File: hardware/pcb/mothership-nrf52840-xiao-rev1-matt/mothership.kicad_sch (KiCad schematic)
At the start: 0 parts

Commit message: pcb: tmp update
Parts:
- added U1: XIAO_nRF52840, symbol A9M0330:MCU_Module__XIAO_nRF52840_NFC-NC
- added U2, U3: MCP23017x-x-SS, Package_SO:SSOP-28_5.3x10.2mm_P0.65mm, symbol A9M0330:IO_Expansion__MCP23017x-x-SS

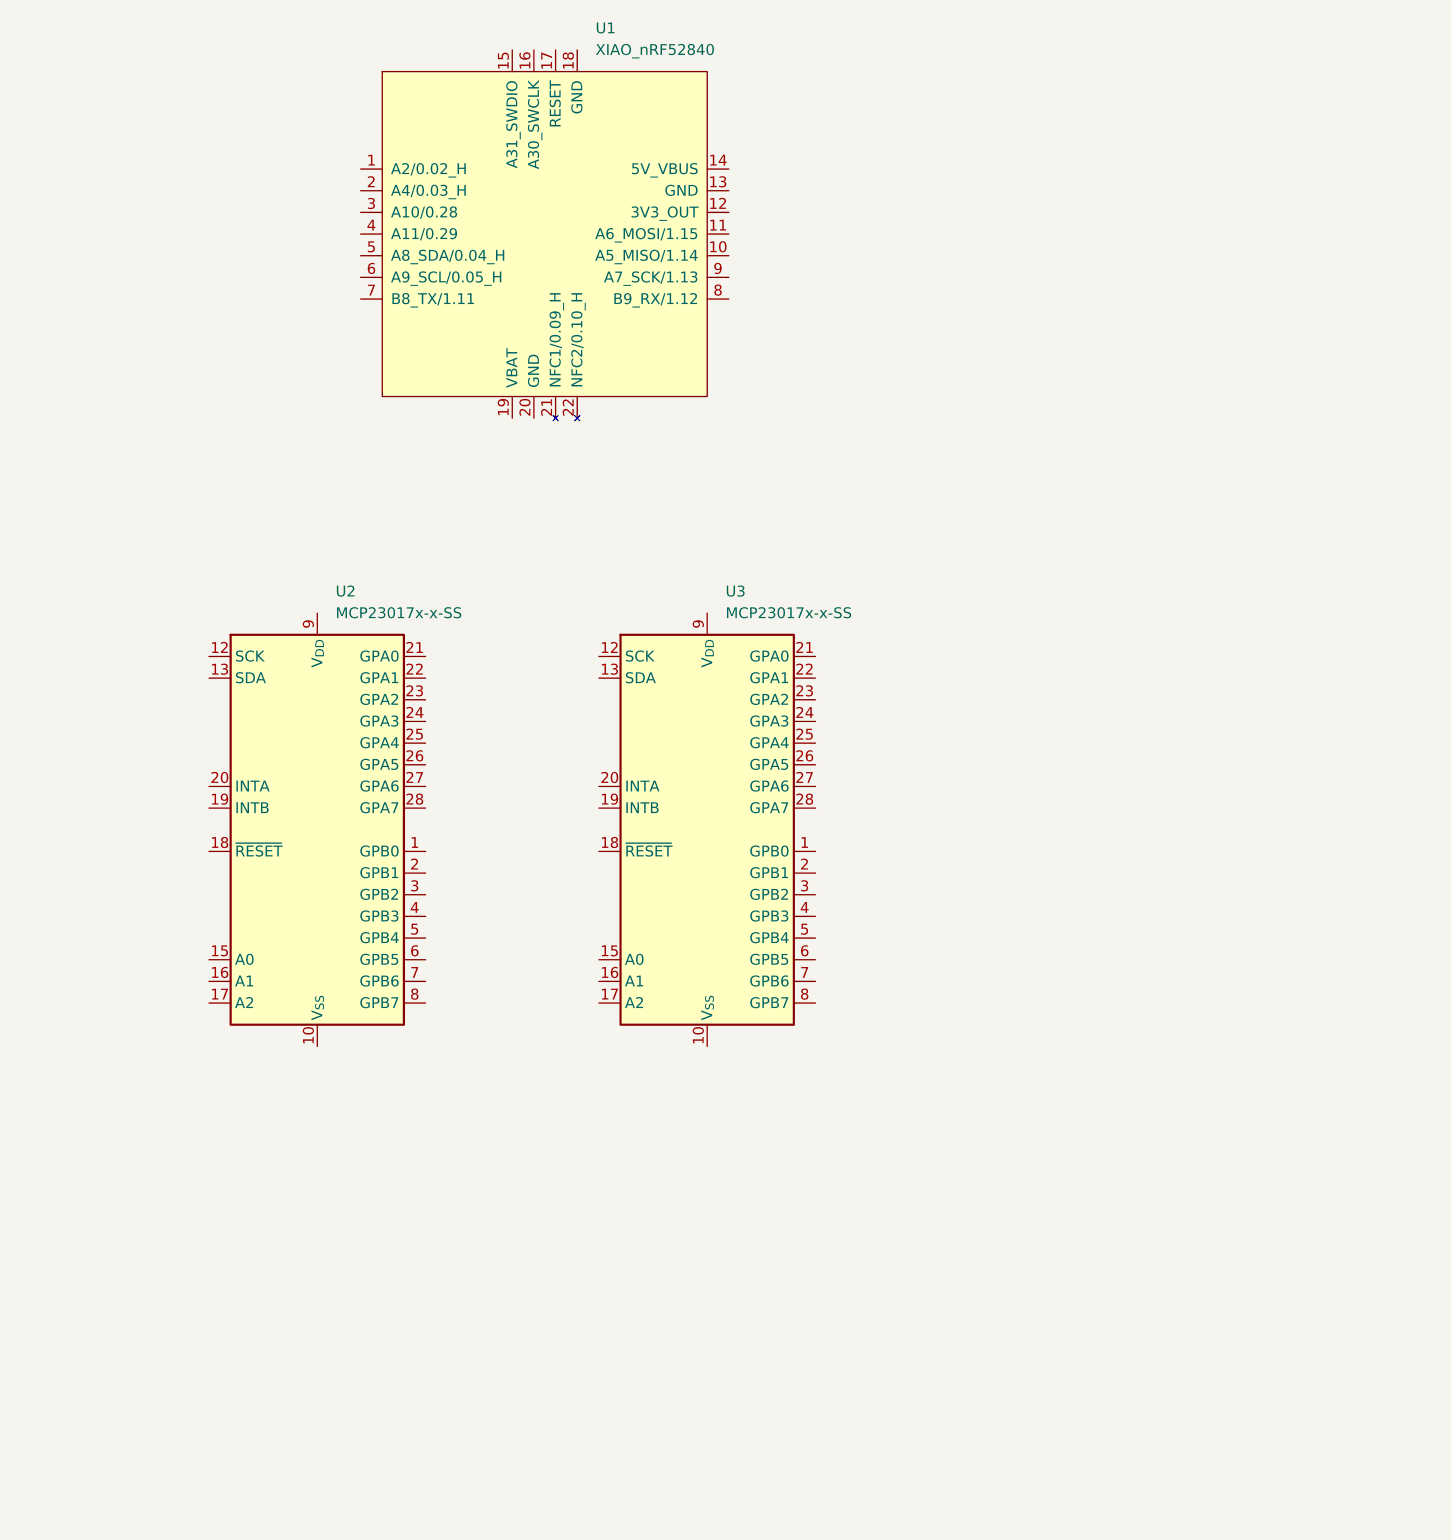
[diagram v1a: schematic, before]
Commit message: sch: add io expander matrix wiring
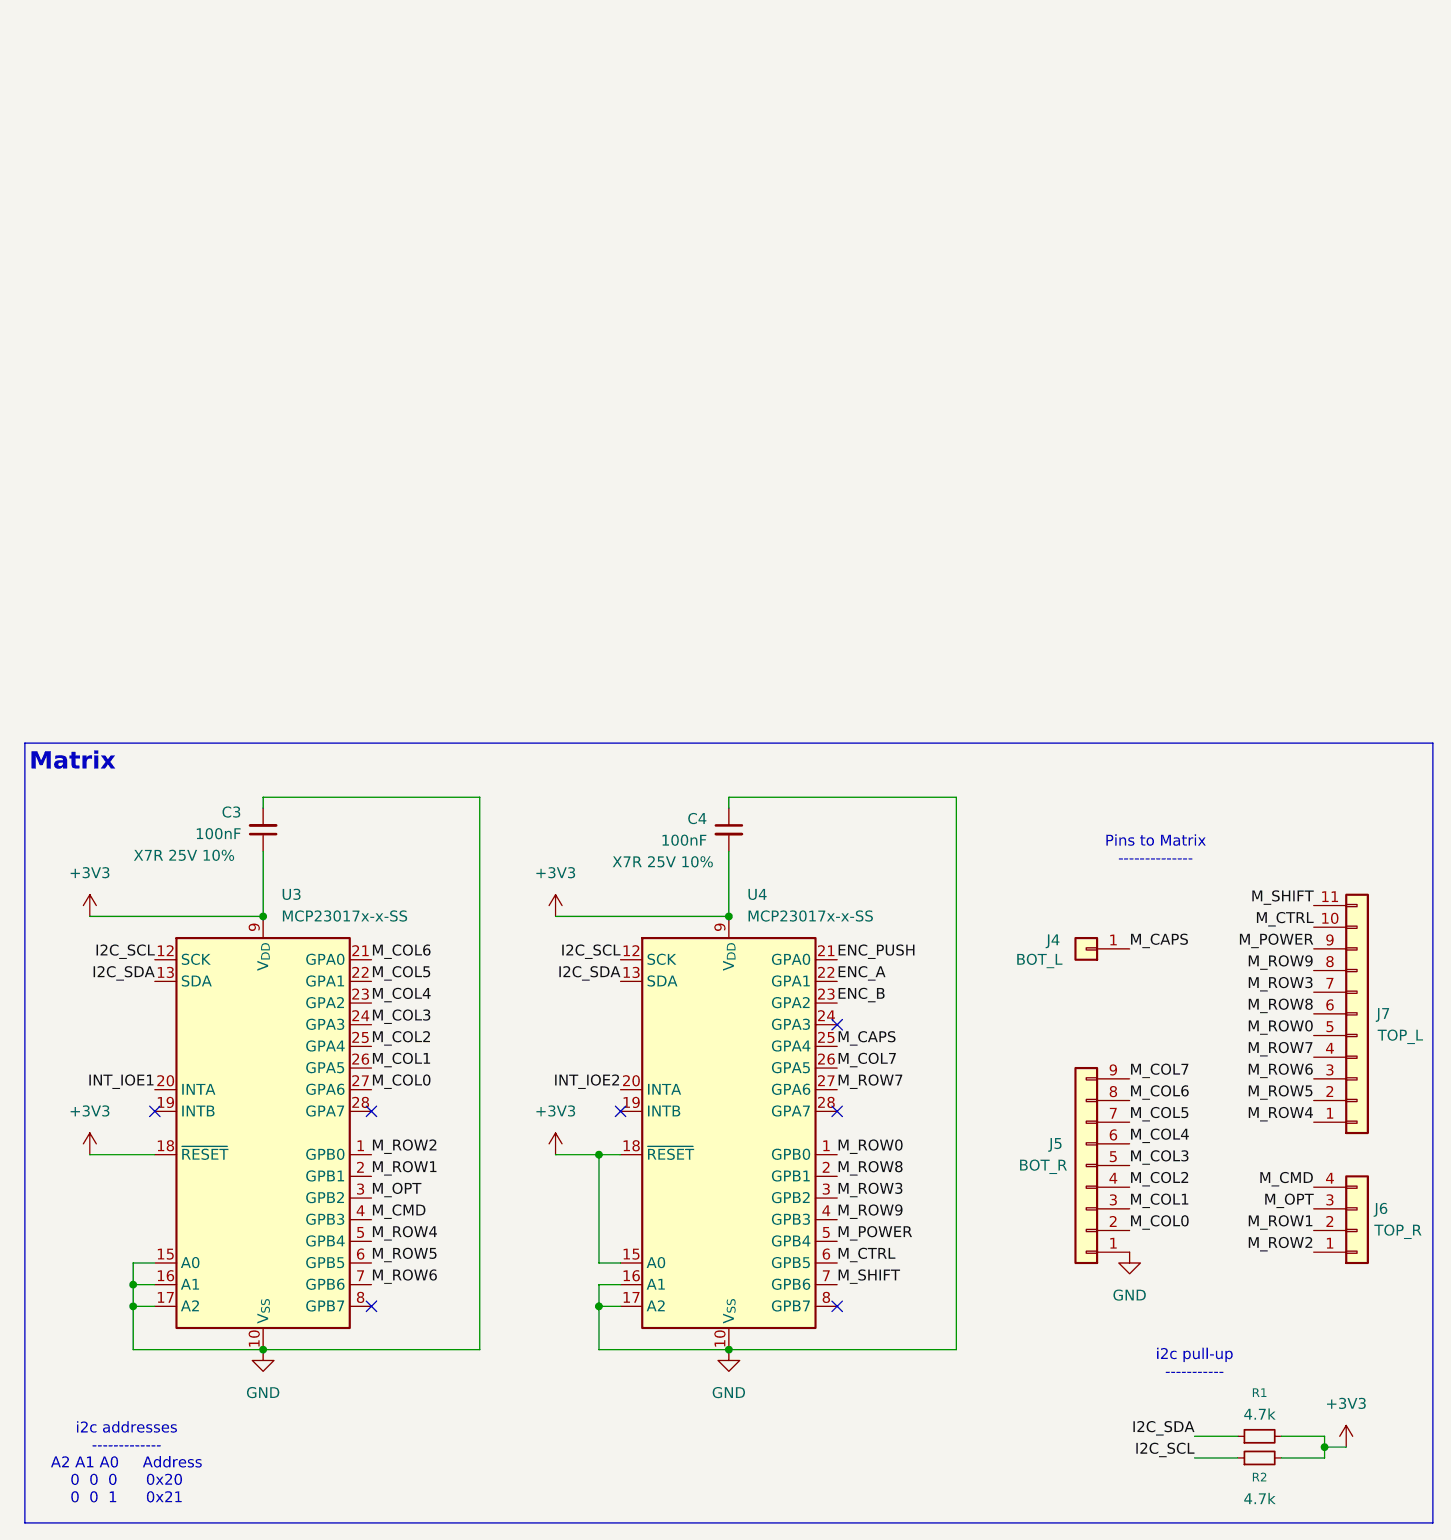
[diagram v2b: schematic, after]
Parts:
- removed U1: XIAO_nRF52840, symbol A9M0330:MCU_Module__XIAO_nRF52840_NFC-NC
- added C3, C4: 100nF, symbol A9M0330:C_Small
- added J4: BOT_L, symbol A9M0330:Conn_01x01
- added J5: BOT_R, symbol A9M0330:Conn_01x09
- added J6: TOP_R, symbol A9M0330:Conn_01x04
- added J7: TOP_L, symbol A9M0330:Conn_01x11
- added R1, R2: 4.7k, symbol A9M0330:R_Small
- renumbered U2 to U3, U3 to U4
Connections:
- net M_ROW2: now reaches U3.1 (GPB0)
- net M_ROW2: now also J6.1 (Pin_1)
- net GND: now reaches U3.10 (V_{SS})
- net GND: now also U3.15 (A0), U3.16 (A1), U3.17 (A2), U4.10 (V_{SS}), U4.16 (A1), U4.17 (A2), C3.2, C4.1, J5.1 (Pin_1)
- net I2C_SCL: now reaches U3.12 (SCK)
- net I2C_SCL: now also U4.12 (SCK), R2.1
- net I2C_SDA: now reaches U3.13 (SDA)
- net I2C_SDA: now also U4.13 (SDA), R1.1
- net +3V3: now reaches U3.18 (~{RESET})
- net +3V3: now also U3.9 (V_{DD}), U4.15 (A0), U4.18 (~{RESET}), U4.9 (V_{DD}), C3.1, C4.2, R1.2, R2.2
- net M_ROW1: now reaches U3.2 (GPB1)
- net M_ROW1: now also J6.2 (Pin_2)
- net INT_IOE1: now reaches U3.20 (INTA)
- net M_COL6: now reaches U3.21 (GPA0)
- net M_COL6: now also J5.8 (Pin_8)
- net M_COL5: now reaches U3.22 (GPA1)
- net M_COL5: now also J5.7 (Pin_7)
- net M_COL4: now reaches U3.23 (GPA2)
- net M_COL4: now also J5.6 (Pin_6)
- net M_COL3: now reaches U3.24 (GPA3)
- net M_COL3: now also J5.5 (Pin_5)
- net M_COL2: now reaches U3.25 (GPA4)
- net M_COL2: now also J5.4 (Pin_4)
- net M_COL1: now reaches U3.26 (GPA5)
- net M_COL1: now also J5.3 (Pin_3)
- net M_COL0: now reaches U3.27 (GPA6)
- net M_COL0: now also J5.2 (Pin_2)
- net M_OPT: now reaches U3.3 (GPB2)
- net M_OPT: now also J6.3 (Pin_3)
- net M_CMD: now reaches U3.4 (GPB3)
- net M_CMD: now also J6.4 (Pin_4)
- net M_ROW4: now reaches U3.5 (GPB4)
- net M_ROW4: now also J7.1 (Pin_1)
- net M_ROW5: now reaches U3.6 (GPB5)
- net M_ROW5: now also J7.2 (Pin_2)
- net M_ROW6: now reaches U3.7 (GPB6)
- net M_ROW6: now also J7.3 (Pin_3)
- net M_ROW0: now reaches U4.1 (GPB0)
- net M_ROW0: now also J7.5 (Pin_5)
- net M_ROW8: now reaches U4.2 (GPB1)
- net M_ROW8: now also J7.6 (Pin_6)
- net INT_IOE2: now reaches U4.20 (INTA)
- net ENC_PUSH: now reaches U4.21 (GPA0)
- net ENC_A: now reaches U4.22 (GPA1)
- net ENC_B: now reaches U4.23 (GPA2)
- net M_CAPS: now reaches U4.25 (GPA4)
- net M_CAPS: now also J4.1 (Pin_1)
- net M_COL7: now reaches U4.26 (GPA5)
- net M_COL7: now also J5.9 (Pin_9)
- net M_ROW7: now reaches U4.27 (GPA6)
- net M_ROW7: now also J7.4 (Pin_4)
- net M_ROW3: now reaches U4.3 (GPB2)
- net M_ROW3: now also J7.7 (Pin_7)
- net M_ROW9: now reaches U4.4 (GPB3)
- net M_ROW9: now also J7.8 (Pin_8)
- net M_POWER: now reaches U4.5 (GPB4)
- net M_POWER: now also J7.9 (Pin_9)
- net M_CTRL: now reaches U4.6 (GPB5)
- net M_CTRL: now also J7.10 (Pin_10)
- net M_SHIFT: now reaches U4.7 (GPB6)
- net M_SHIFT: now also J7.11 (Pin_11)
- no-connect marks 0 -> 7
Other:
- note added: "Matrix"
- note added: "Pins to Matrix --------------"
- note added: "i2c addresses ------------- A2 A1 A0 Address 0 0 0 0x20 0 0 1 0x21"
- note added: "i2c pull-up -----------"
- moved on the sheet: U3, U4

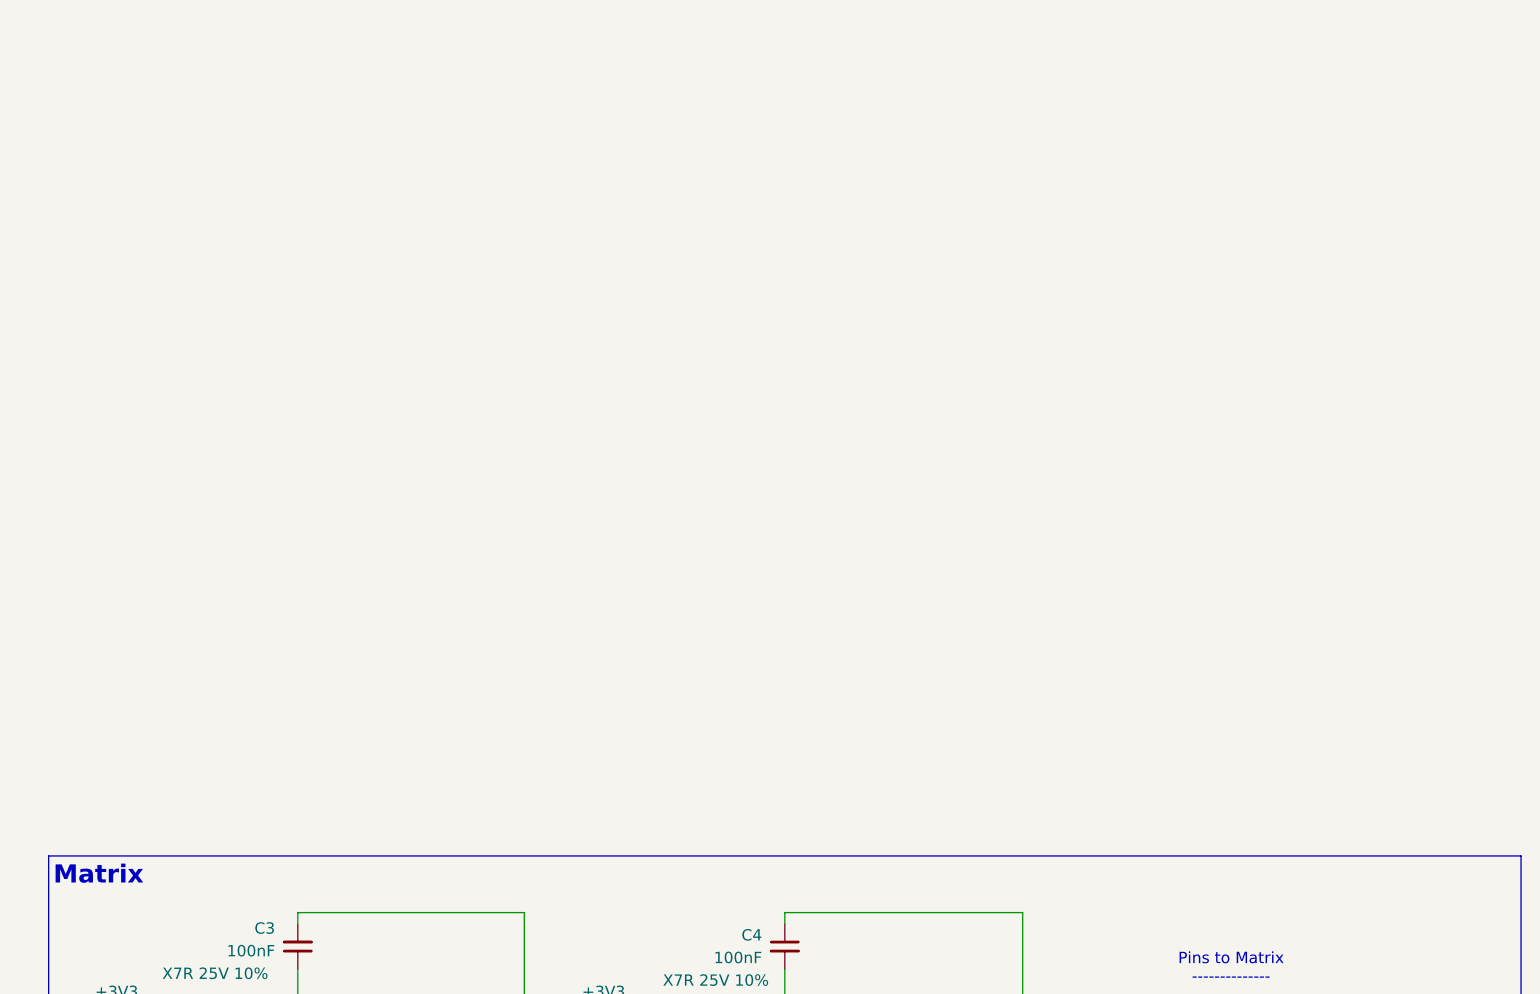
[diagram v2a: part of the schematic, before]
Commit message: sch: add usb protection circuit
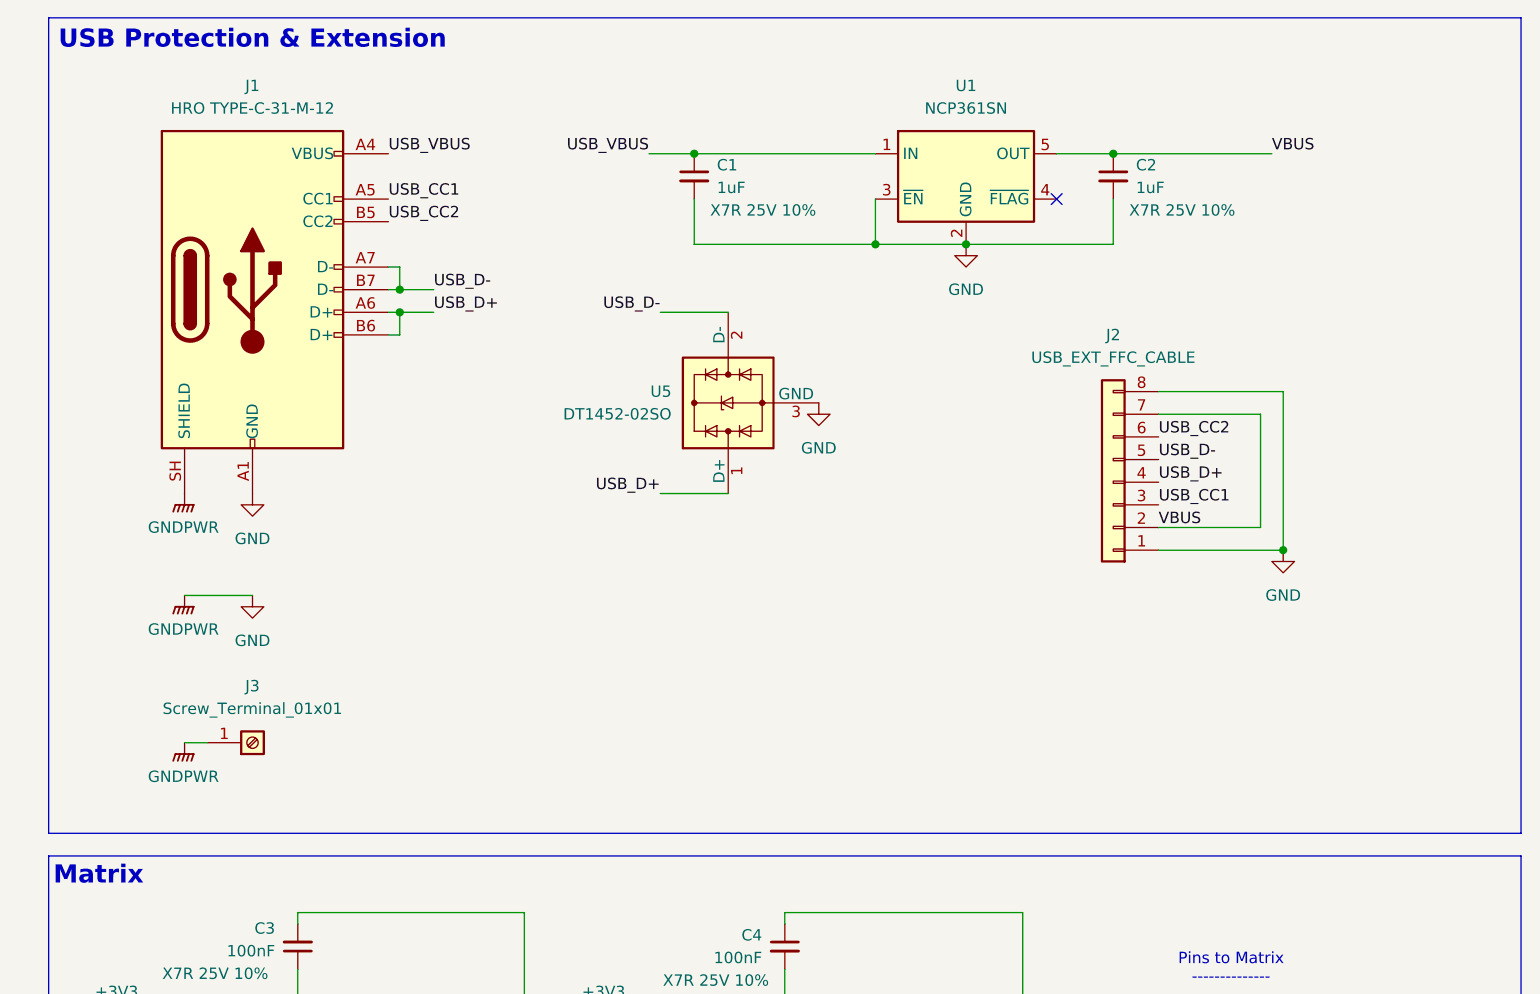
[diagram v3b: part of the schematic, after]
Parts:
- added C1, C2: 1uF, symbol A9M0330:C_Small
- added J1: HRO TYPE-C-31-M-12, symbol A9M0330:USB_C_Receptacle_USB2.0_14P
- added J2: USB_EXT_FFC_CABLE, symbol A9M0330:Conn_01x08
- added J3: Screw_Terminal_01x01, symbol A9M0330:Screw_Terminal_01x01
- added U1: NCP361SN, Package_SO:TSOP-5_1.65x3.05mm_P0.95mm, symbol A9M0330:Protection_Power__NCP361SN
- added U5: DT1452-02SO, Package_TO_SOT_SMD:SOT-23, symbol A9M0330:Protection_ESD__DT1452-02SO
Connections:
- net GND: now also C1.2, C2.2, J1.A1 (GND), J1.A12 (GND), J1.B1 (GND), J1.B12 (GND), J1.SH (SHIELD), J2.1 (Pin_1), J2.8 (Pin_8), J3.1 (Pin_1), U1.2 (GND), U1.3 (~{EN}), U5.3 (GND)
- new net USB_CC1: J1.A5 (CC1), J2.3 (Pin_3)
- new net USB_CC2: J1.B5 (CC2), J2.6 (Pin_6)
- new net USB_D+: J1.A6 (D+), J1.B6 (D+), J2.4 (Pin_4), U5.1 (D+)
- new net USB_D-: J1.A7 (D-), J1.B7 (D-), J2.5 (Pin_5), U5.2 (D-)
- new net USB_VBUS: C1.1, J1.A4 (VBUS), J1.A9 (VBUS), J1.B4 (VBUS), J1.B9 (VBUS), U1.1 (IN)
- new net VBUS: C2.1, J2.2 (Pin_2), J2.7 (Pin_7), U1.5 (OUT)
- no-connect marks 7 -> 8
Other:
- note added: "USB Protection & Extension"
